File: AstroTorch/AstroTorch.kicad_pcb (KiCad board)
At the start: 2 copper layers, 23 parts, among them J1 Conn_01x02_Pin, Q1 IRLML2060, Q2 IRLML2060, SW1 RotaryEncoder_Switch, U1 MCP1703Ax-330xxTT, U2 ATtiny24A-SS

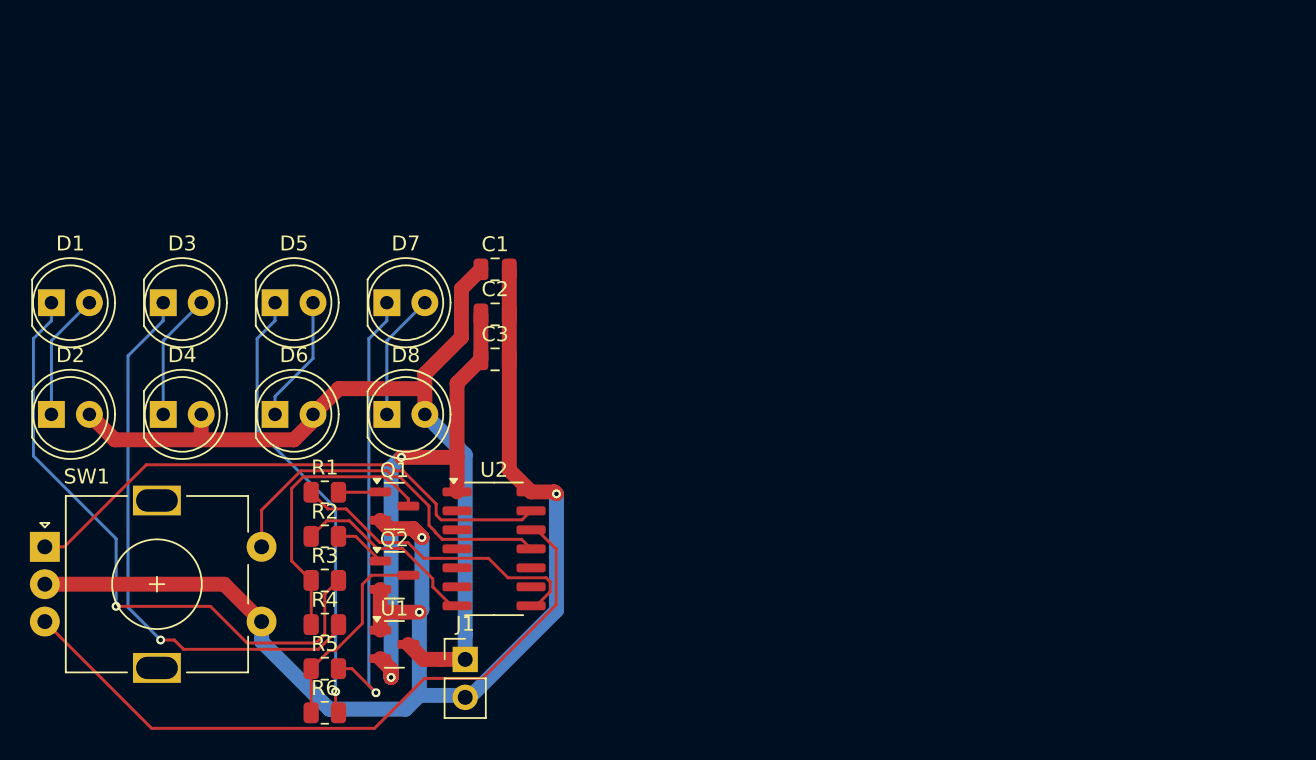
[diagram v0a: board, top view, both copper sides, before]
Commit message: Added case
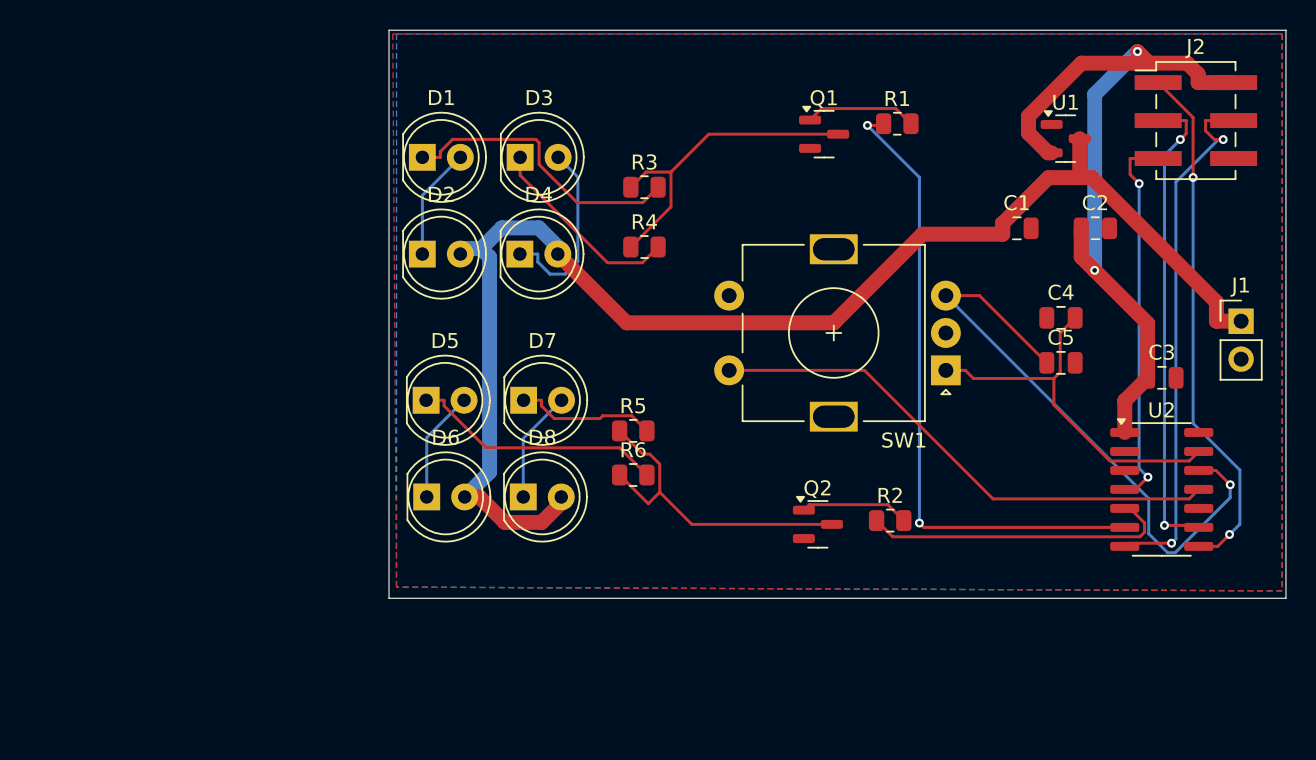
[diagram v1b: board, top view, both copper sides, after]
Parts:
- added C4: 10n, Capacitor_SMD:C_0805_2012Metric, F.Cu at (122.5, 55.0)
- added C5: 10n, Capacitor_SMD:C_0805_2012Metric, F.Cu at (122.5, 58.0)
- added J2: Conn_02x03_Odd_Even, Connector_PinHeader_2.54mm:PinHeader_2x03_P2.54mm_Vertical_SMD, F.Cu at (131.5, 41.8)
- C3: value 1u -> 10n
- Q1, Q2: value IRLML2060 -> IRLML 2502
- moved SW1 61.4 mm to (114.8, 58.5), turned to 180 degrees
- moved J1 56.6 mm to (134.5, 55.2)
- moved U1 56.2 mm to (122.8, 43.0)
- moved R1 45.5 mm to (111.5, 42.0)
- moved U2 44.8 mm to (129.2, 66.5)
- moved C3 44.6 mm to (129.2, 59.0)
- moved C2 40.6 mm to (124.8, 49.0)
- moved Q1 38.0 mm to (106.6, 42.7)
- moved R2 37.8 mm to (111.0, 68.5)
- moved C1 35.0 mm to (119.5, 49.0)
- moved R3 33.9 mm to (94.6, 46.2)
- moved R4 33.1 mm to (94.6, 50.2)
- moved Q2 28.5 mm to (106.2, 68.8)
- moved D2 27.0 mm to (79.7, 50.7)
- moved D1 26.7 mm to (79.7, 44.2)
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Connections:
- R1 pad 1: Net-(U2-PA5) -> Net-(U2-PA7)
- R2 pad 1: Net-(U2-PA6) -> Net-(U2-PB2)
- U2 pad 4: unconnected-(U2-~{RESET}/PB3-Pad4) -> RESET
- U2 pad 5: unconnected-(U2-PB2-Pad5) -> Net-(U2-PB2)
- U2 pad 6: unconnected-(U2-PA7-Pad6) -> Net-(U2-PA7)
- U2 pad 7: Net-(U2-PA6) -> MOSI
- U2 pad 8: Net-(U2-PA5) -> MISO
- U2 pad 9: unconnected-(U2-PA4-Pad9) -> SCK
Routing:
- net GND: track 88.9 -> 0.00 mm, vias 3 -> 0
- net Net-(U2-PA7): track 0.00 -> 43.0 mm, vias 0 -> 2
- net MOSI: track 0.00 -> 35.8 mm, vias 0 -> 2
- net MISO: track 0.00 -> 35.2 mm, vias 0 -> 2
- net +9V: track 59.5 -> 93.3 mm
- net SCK: track 0.00 -> 31.9 mm, vias 0 -> 2
- net RESET: track 0.00 -> 25.6 mm, vias 0 -> 2
- net Net-(D3-K): track 37.5 -> 13.3 mm, vias 1 -> 0
- net Net-(D1-K): track 42.3 -> 19.5 mm, vias 1 -> 0
- net Net-(D7-K): track 30.3 -> 9.47 mm, vias 1 -> 0
- net Net-(U2-PB2): track 0.00 -> 20.9 mm
- net Net-(U2-PA5): track 20.8 -> 0.00 mm
- net +3.3V: track 33.9 -> 52.3 mm
- net Net-(D5-K): track 30.2 -> 17.1 mm, vias 1 -> 0
- net Net-(U2-PA6): track 12.9 -> 0.00 mm
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- added copper zone on B.Cu, net GND
- added copper zone on F.Cu, net GND
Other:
- board outline added: 60 x 38 mm
